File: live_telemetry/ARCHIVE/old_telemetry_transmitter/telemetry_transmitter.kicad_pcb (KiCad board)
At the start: 2 copper layers, 58.4 x 61 mm, 46 parts, among them J1 Programming Header, J2 G125-MH104M4-04AD000P, J3 RFD900x, Q1 PJA3405, Q2 TSM2306CX, U1 PIC18F26K83, U2 MCP2562, U3 TPS56339DDC, U4 INA180, U5 SPX3819M5-L-3-3/TR, Y1 ABM8G-12.000MHZ-18-D2Y-T

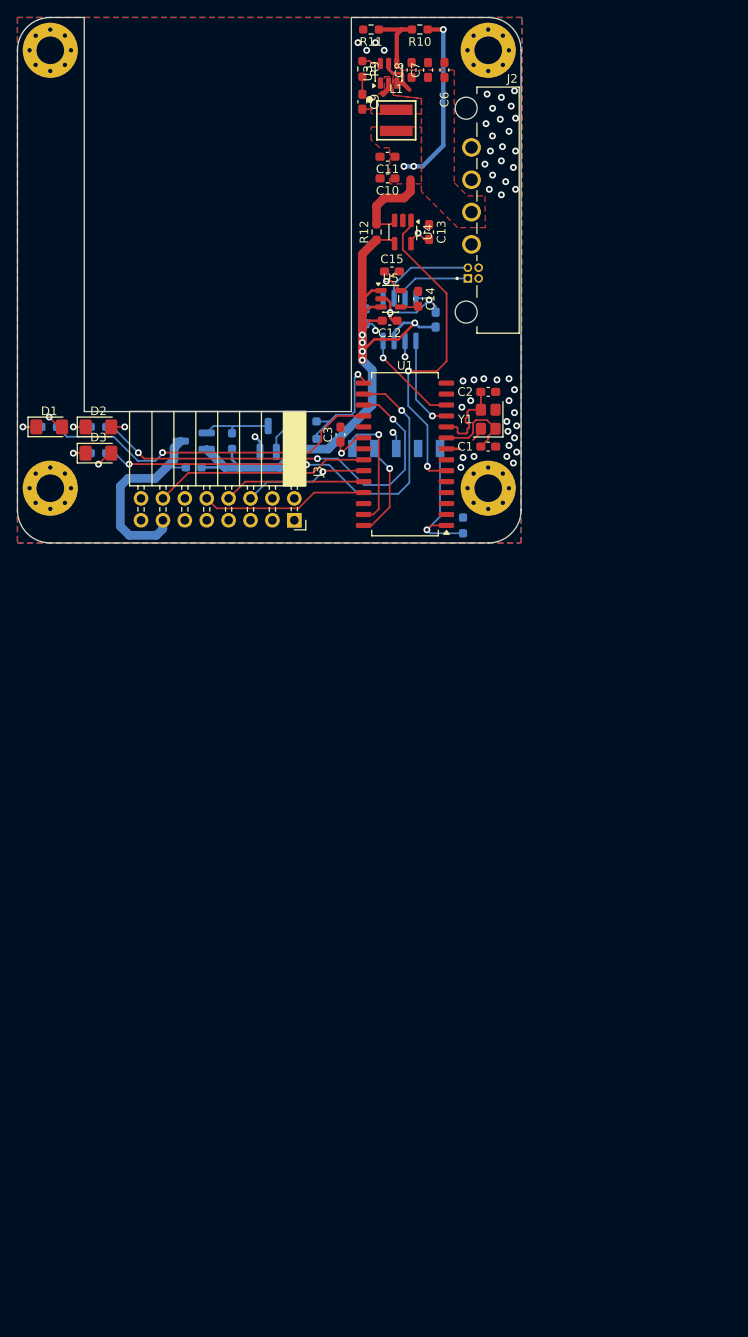
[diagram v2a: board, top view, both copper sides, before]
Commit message: minor layout edits, silkscreens placed, logo and board name added, prod files pdf and .step created
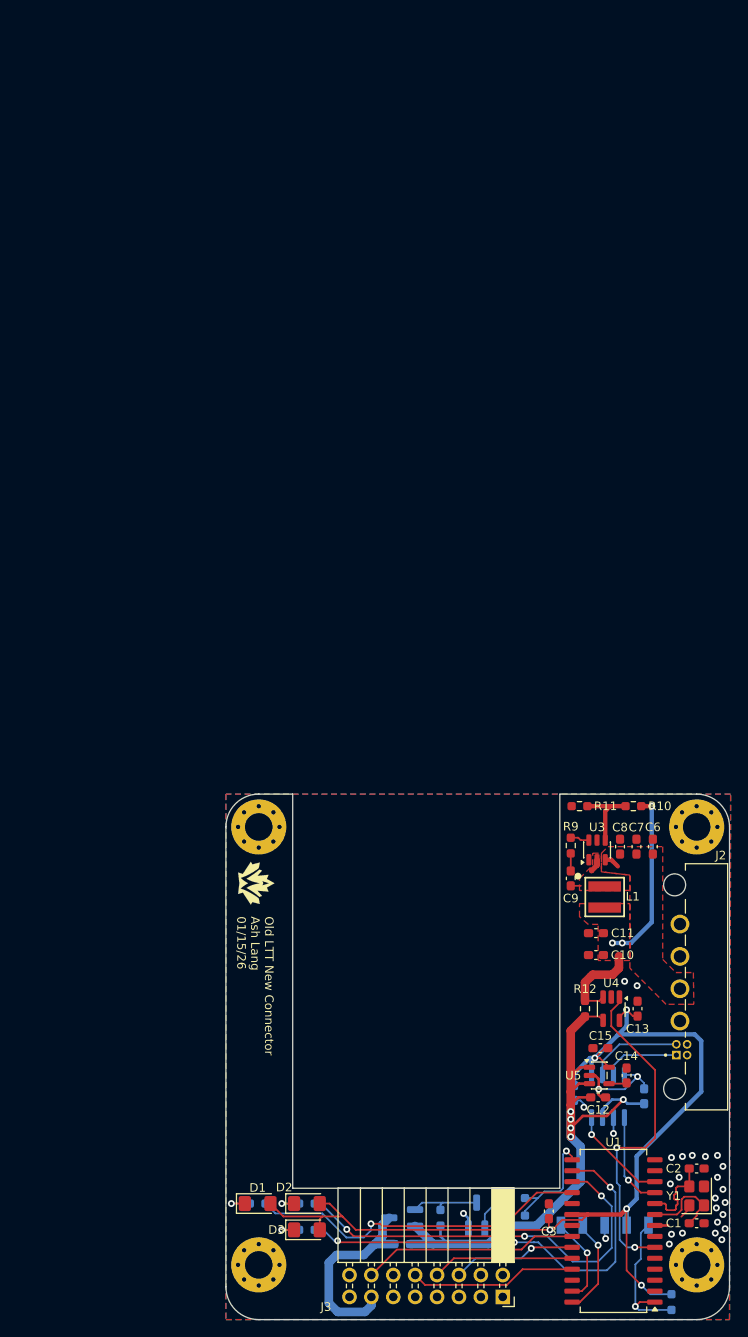
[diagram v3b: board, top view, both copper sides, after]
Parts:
- added G***: LOGO, Team_Logo:Logo_SilkScreen_5mm, F.Cu at (112.0, 83.9)
- R12: value 0.02R -> 0.03R
- U4: value INA180 -> INA180A3
- moved R10 93.4 mm to (155.8, 75.0)
- moved H1 93.3 mm to (112.3, 128.2)
- moved H2 93.3 mm to (163.1, 128.2)
- moved J3 93.3 mm to (140.6, 131.9)
- moved Q2 93.3 mm to (137.6, 122.5)
- moved R8 93.3 mm to (142.3, 122.5)
- moved C1 93.3 mm to (163.1, 123.4)
- moved C12 93.3 mm to (151.7, 108.8)
- moved C14 93.3 mm to (155.0, 106.2)
- moved C3 93.3 mm to (146.0, 122.0)
- moved C4 93.3 mm to (148.9, 108.3)
- moved C6 93.3 mm to (158.0, 79.7)
- moved C7 93.3 mm to (156.1, 79.7)
- moved C8 93.3 mm to (154.2, 79.7)
- moved D1 93.3 mm to (112.2, 121.1)
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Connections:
- U3 pad 5: +12V -> unconnected-(U3-EN-Pad5)
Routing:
- net +3V3: track 17.4 -> 121.9 mm, vias 6 -> 5
- net /ICSPCLK: track 15.0 -> 10.3 mm
- net +12V: track 5.28 -> 1.78 mm
- net /power/CURR_LTT: track 38.3 -> 39.0 mm
- net Net-(U4-IN+): track 31.3 -> 30.7 mm
- net Net-(U3-FB): track 8.01 -> 8.60 mm
- net GND: track 24.9 -> 24.5 mm, vias 53 -> 30
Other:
- board text added: "Old LTT New Connector Ash Lang 01/15/26"
- board text added: "~{MCLR} ->"

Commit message: update paths for 3d models
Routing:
- added copper zone on B.Cu, net GND
- removed copper zone on B.Cu, net +3V3
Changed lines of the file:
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@@
-	)
-	(zone
-		(net 1)
-		(net_name "GND")
-		(layer "F.Cu")
-		(hatch edge 0.5)
-		(connect_pads
-			(clearance 0.1524)
-		)
-		(min_thickness 0.25)
-		(filled_areas_thickness no)
-		(fill yes
-			(thermal_gap 0.5)
-			(thermal_bridge_width 0.5)
-		)
-		(polygon
-			(pts
-				(xy 167.0558 73.5838) (xy 108.5088 73.5838) (xy 108.5088 134.5438) (xy 166.9288 134.5438)
-			)
-		)
 	)
 	(zone
@@
 	)
 	(zone
-		(net 4)
-		(net_name "+3V3")
-		(layer "B.Cu")
+		(net 1)
+		(net_name "GND")
+		(layers "F.Cu" "B.Cu")
 		(hatch edge 0.5)
 		(connect_pads

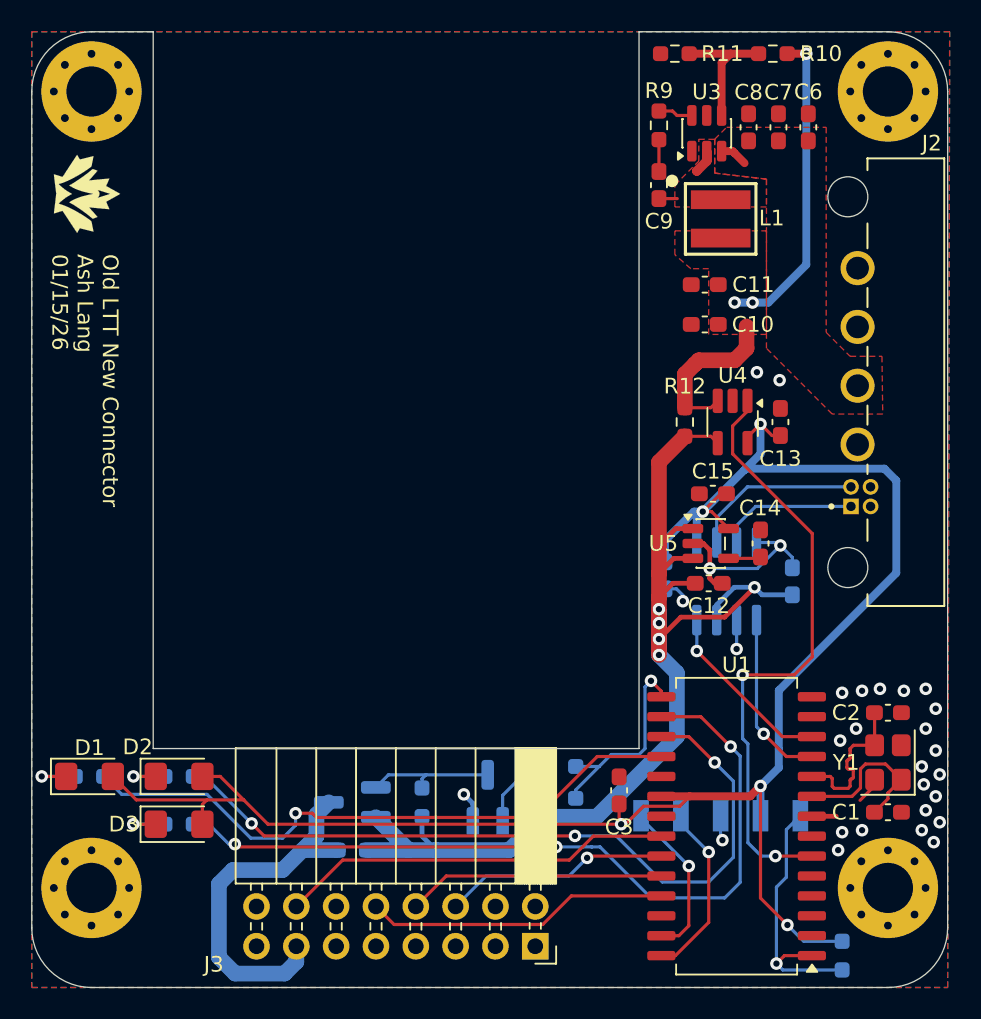
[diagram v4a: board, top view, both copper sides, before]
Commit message: add RFD900x and assembly, add rounded corners, regen gerbers and step
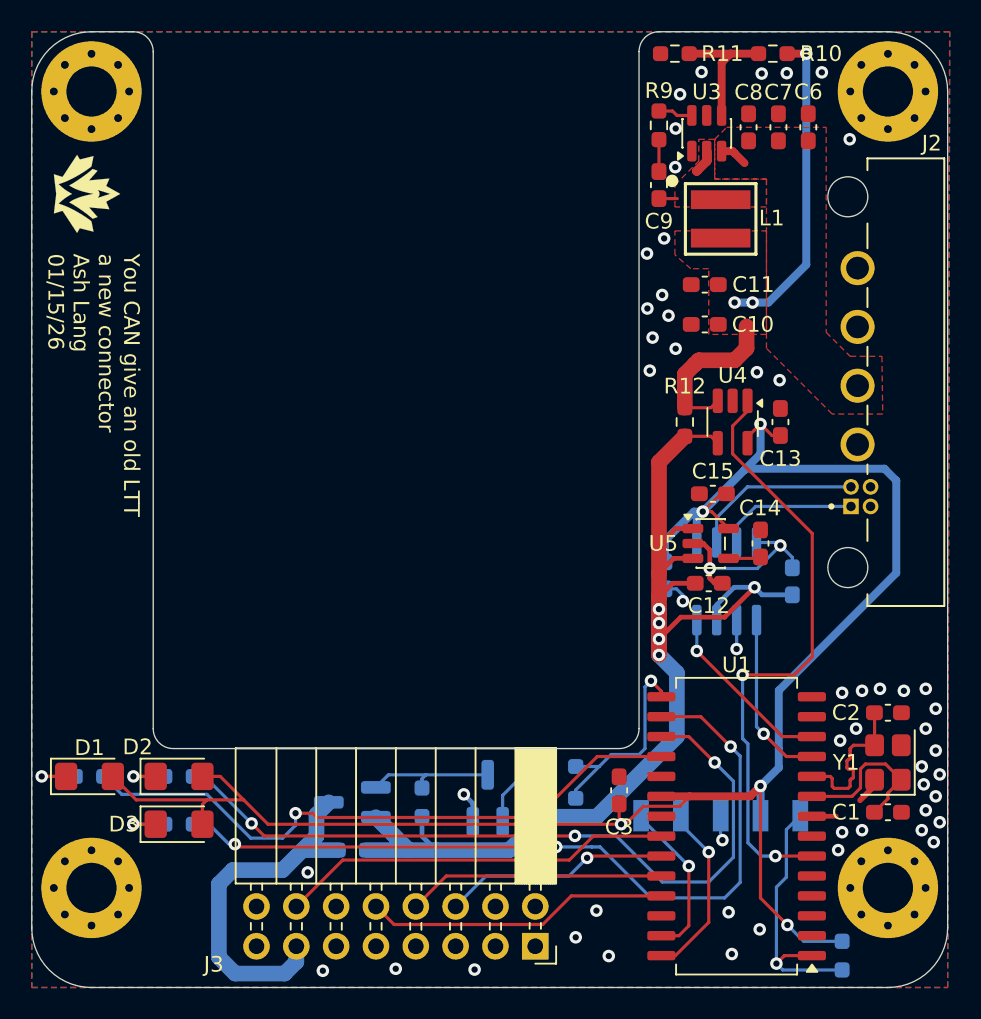
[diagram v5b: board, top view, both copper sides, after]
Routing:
- net GND: vias 30 -> 56
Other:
- outline, holes or cut-outs redrawn
- board text added: "You CAN give an old LTT a new connector Ash Lang 01/15/26"
- board text removed: "Old LTT New Connector Ash Lang 01/15/26"
